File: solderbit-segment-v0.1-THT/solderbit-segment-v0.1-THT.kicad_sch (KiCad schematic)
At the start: 13 parts, among them J1 Conn_01x05_Pin, U1 PCF8574AT, U2 PCF8574N

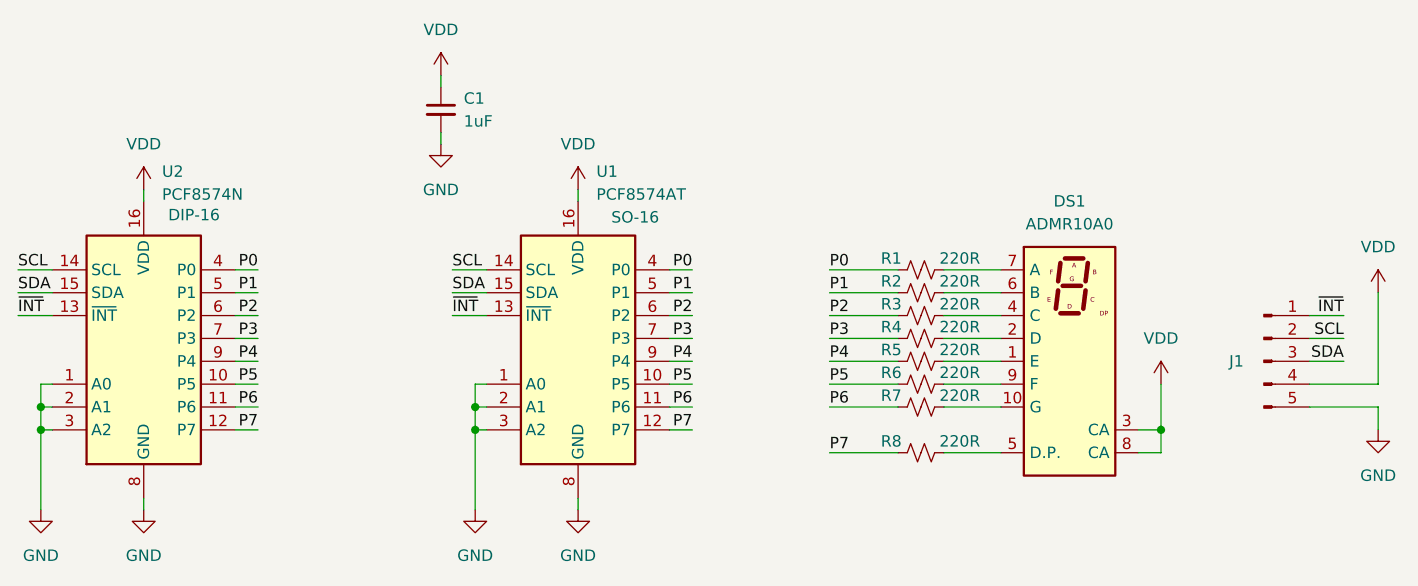
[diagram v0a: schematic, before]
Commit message: PCB with dual footprints
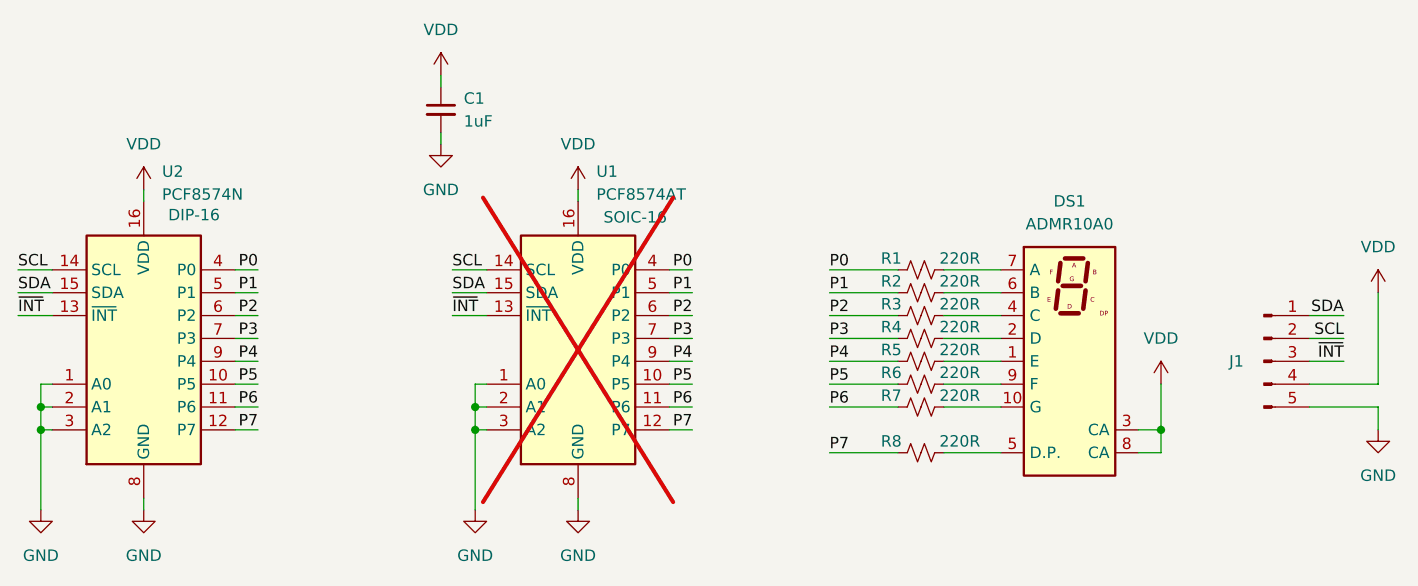
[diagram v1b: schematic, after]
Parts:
- U1: Package SO-16 -> SOIC-16; now not fitted
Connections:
- net SDA: now also J1.1 (Pin_1); no longer J1.3 (Pin_3)
- net ~{INT}: now also J1.3 (Pin_3); no longer J1.1 (Pin_1)
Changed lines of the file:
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@@
+		)
+	)
+	(label "SDA"
+		(at 209.55 85.09 180)
+		(effects
+			(font
+				(size 1.27 1.27)
+			)
+			(justify right bottom)
 		)
 	)
@@
 		)
 	)
-	(label "~{INT}"
-		(at 209.55 85.09 180)
-		(effects
-			(font
-				(size 1.27 1.27)
-			)
-			(justify right bottom)
-		)
-	)
-	(label "SDA"
-		(at 209.55 90.17 180)
-		(effects
-			(font
-				(size 1.27 1.27)
-			)
-			(justify right bottom)
-		)
-	)
 	(label "P3"
 		(at 137.16 87.63 180)
@@
 		)
 	)
+	(label "~{INT}"
+		(at 209.55 90.17 180)
+		(effects
+			(font
+				(size 1.27 1.27)
+			)
+			(justify right bottom)
+		)
+	)
 	(symbol
 		(lib_id "power:VDD")
@@
 		(exclude_from_sim no)
 		(in_bom yes)
-		(on_board yes)
-		(dnp no)
+		(on_board no)
+		(dnp yes)
 		(property "Reference" "U1"
 			(at 126.492 69.088 0)
@@
 			)
 		)
-		(property "Package" "SO-16"
+		(property "Package" "SOIC-16"
 			(at 130.81 74.168 0)
 			(effects
